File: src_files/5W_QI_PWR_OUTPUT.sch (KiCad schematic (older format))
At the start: 48 parts, among them IC3 P9038, U15 24AA64T-I/OT, U16 BRCS120N02ZJ

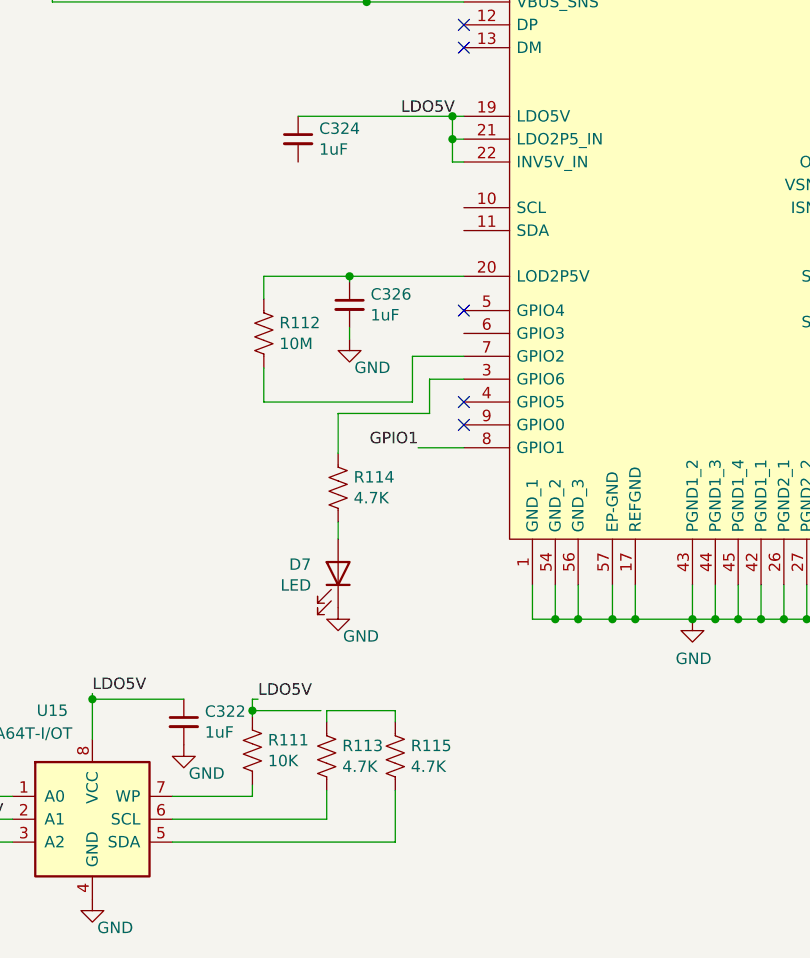
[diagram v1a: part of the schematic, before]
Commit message: updates rules check and associations
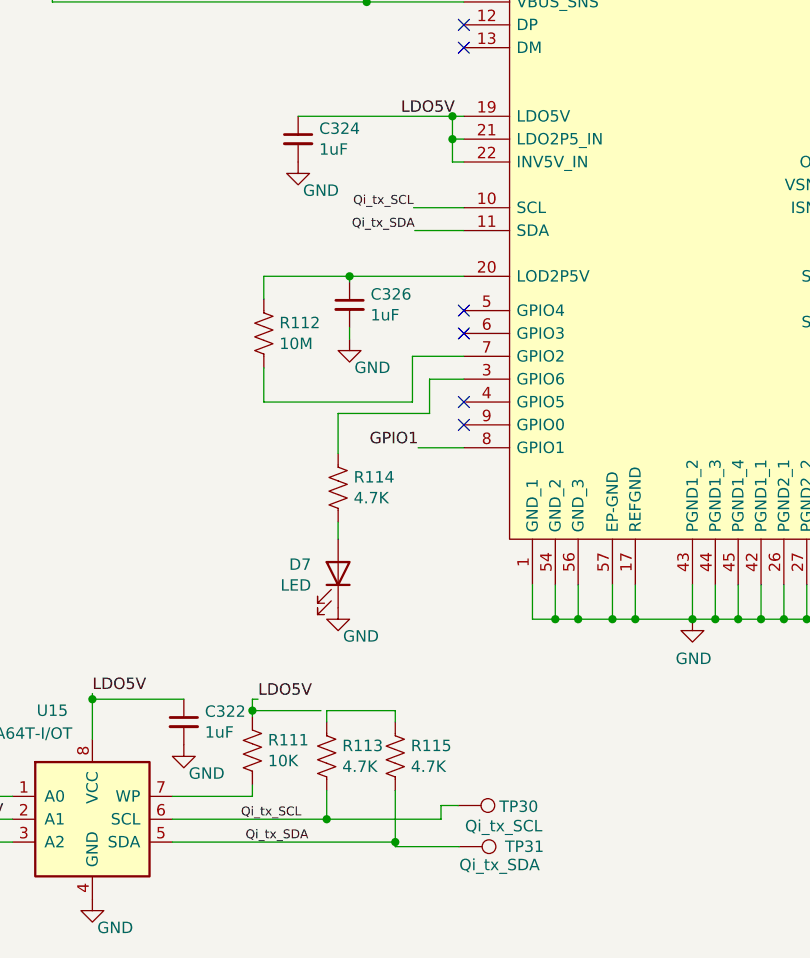
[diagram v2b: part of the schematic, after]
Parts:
- added TP30: Qi_tx_SCL, TestPoint:TestPoint_Pad_D1.0mm, symbol Connector:TestPoint
- added TP31: Qi_tx_SDA, TestPoint:TestPoint_Pad_D1.0mm, symbol Connector:TestPoint
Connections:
- net GND: now also C324.2
- net Qi_tx_SCL: now reaches IC3.10 (SCL)
- net Qi_tx_SCL: now also R113.2, U15.6 (SCL), TP30.1
- net Qi_tx_SDA: now reaches IC3.11 (SDA)
- net Qi_tx_SDA: now also R115.2, U15.5 (SDA), TP31.1
- no-connect marks 7 -> 8
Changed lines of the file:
@@
 $Descr A4 11693 8268
 encoding utf-8
-Sheet 16 17
+Sheet 15 17
 Title ""
 Date ""
@@
 	2650 6600 1675 6600
 Wire Wire Line
-	1675 6500 2350 6500
-Wire Wire Line
 	2350 6500 2350 6375
 Text Label 1325 5950 0    50   ~ 0
@@
 	8975 2800 9125 2800
 Connection ~ 8975 4075
+NoConn ~ 2950 4375
+Text Label 2730 3825 2    39   ~ 0
+Qi_tx_SCL
+Text Label 2735 3925 2    39   ~ 0
+Qi_tx_SDA
+Wire Wire Line
+	2950 3825 2730 3825
+Wire Wire Line
+	2950 3925 2735 3925
+Text Label 1975 6500 0    39   ~ 0
+Qi_tx_SCL
+Text Label 1995 6600 0    39   ~ 0
+Qi_tx_SDA
+$Comp
+L Connector:TestPoint TP?
+U 1 1 640B8AE1
+P 2925 6440
+AR Path="/61C73AB6/640B8AE1" Ref="TP?"  Part="1"
+AR Path="/62F6D336/640B8AE1" Ref="TP?"  Part="1"
+AR Path="/6823D52E/640B8AE1" Ref="TP?"  Part="1"
+AR Path="/626A6204/640B8AE1" Ref="TP30"  Part="1"
+F 0 "TP30" V 2930 6620 50  0000 L CNN
+F 1 "Qi_tx_SCL" V 3015 6470 50  0000 L CNN
+F 2 "TestPoint:TestPoint_Pad_D1.0mm" H 3125 6440 50  0001 C CNN
+F 3 "~" H 3125 6440 50  0001 C CNN
+	1    2925 6440
+	0    1    1    0
+$EndComp
+$Comp
+L Connector:TestPoint TP?
+U 1 1 640B8AE7
+P 2930 6620
+AR Path="/61C73AB6/640B8AE7" Ref="TP?"  Part="1"
+AR Path="/62F6D336/640B8AE7" Ref="TP?"  Part="1"
+AR Path="/6823D52E/640B8AE7" Ref="TP?"  Part="1"
+AR Path="/626A6204/640B8AE7" Ref="TP31"  Part="1"
+F 0 "TP31" V 2930 6820 50  0000 L CNN
+F 1 "Qi_tx_SDA" V 3010 6620 50  0000 L CNN
+F 2 "TestPoint:TestPoint_Pad_D1.0mm" H 3130 6620 50  0001 C CNN
+F 3 "~" H 3130 6620 50  0001 C CNN
+	1    2930 6620
+	0    1    1    0
+$EndComp
+Wire Wire Line
+	2930 6620 2650 6620
+Wire Wire Line
+	2650 6620 2650 6600
+Connection ~ 2650 6600
+Wire Wire Line
+	2850 6500 2850 6440
+Wire Wire Line
+	2850 6440 2925 6440
+Wire Wire Line
+	1675 6500 2350 6500
+Connection ~ 2350 6500
+Wire Wire Line
+	2350 6500 2850 6500
+$Comp
+L power:GND #PWR0271
+U 1 1 64105B12
+P 2225 3625
+F 0 "#PWR0271" H 2225 3375 50  0001 C CNN
+F 1 "GND" H 2325 3500 50  0000 C CNN
+F 2 "" H 2225 3625 50  0001 C CNN
+F 3 "" H 2225 3625 50  0001 C CNN
+	1    2225 3625
+	1    0    0    -1
+$EndComp
 $EndSCHEMATC

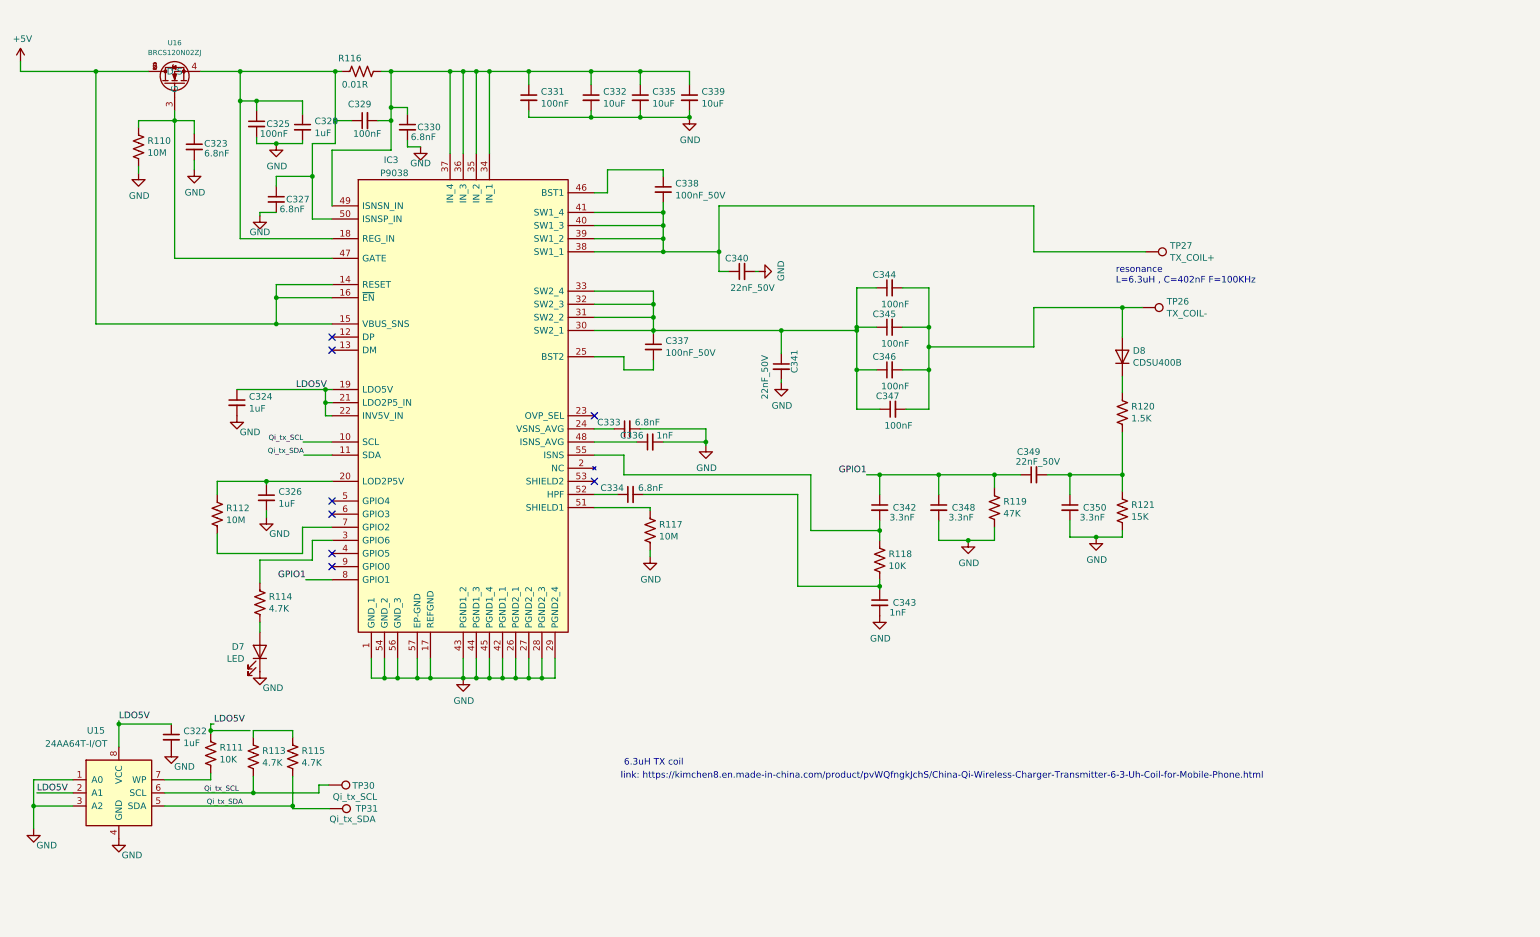
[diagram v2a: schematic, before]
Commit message: update schematic
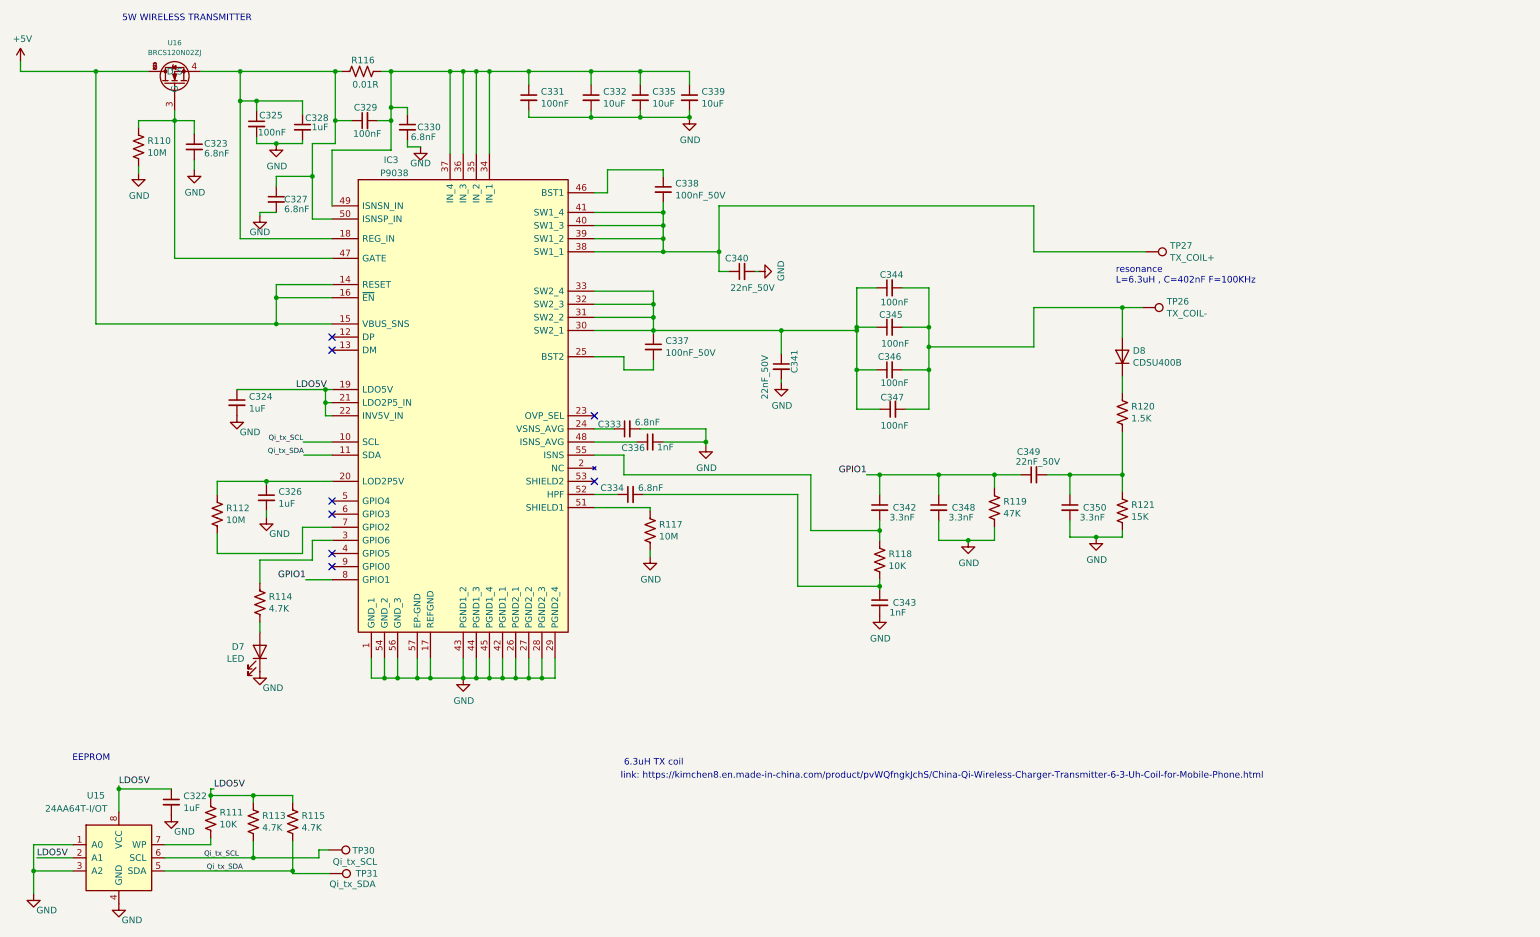
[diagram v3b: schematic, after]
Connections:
- net LDO5V: now also R113.1, R115.1
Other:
- note added: "5W WIRELESS TRANSMITTER"
- note added: "EEPROM"
- moved on the sheet: C322, R111, R113, R115, TP30, TP31, U15
